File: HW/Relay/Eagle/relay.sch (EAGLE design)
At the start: 41 parts, among them IC2 DS18B20, K2 CQ1-12V, Q1A MMBT3904, Q1B MMBT3904, T1 BC847, U3 MCP16311

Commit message: Add files via upload
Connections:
- new net N$3: NC1.1, U3.VFB
- net N$28: no longer NC1.1, U3.VFB
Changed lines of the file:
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@@
 <wire x1="8.382" y1="264.16" x2="8.382" y2="267.716" width="0.1524" layer="91"/>
 <junction x="8.382" y="267.716"/>
-<pinref part="NC1" gate="G$1" pin="2"/>
-<wire x1="2.032" y1="263.906" x2="2.032" y2="267.716" width="0.1524" layer="91" style="shortdash"/>
-<junction x="2.032" y="267.716"/>
 <pinref part="SUPPLY11" gate="G$1" pin="VCC"/>
 <wire x1="-33.274" y1="281.432" x2="-33.274" y2="267.716" width="0.1524" layer="91"/>
 <junction x="-33.274" y="267.716"/>
 <pinref part="L1" gate="G$1" pin="1"/>
+<pinref part="NC1" gate="G$1" pin="2"/>
+<wire x1="2.032" y1="263.906" x2="2.032" y2="267.716" width="0.1524" layer="91"/>
+<junction x="2.032" y="267.716"/>
 </segment>
 <segment>
@@
 <net name="N$28" class="0">
 <segment>
-<pinref part="U3" gate="G$1" pin="VFB"/>
-<wire x1="75.184" y1="257.556" x2="75.184" y2="238.76" width="0.1524" layer="91"/>
-<wire x1="75.184" y1="238.76" x2="27.94" y2="238.76" width="0.1524" layer="91"/>
-<wire x1="27.94" y1="238.76" x2="27.94" y2="251.46" width="0.1524" layer="91"/>
 <pinref part="R15" gate="G$1" pin="1"/>
-<wire x1="27.94" y1="251.46" x2="8.382" y2="251.46" width="0.1524" layer="91"/>
-<wire x1="8.382" y1="251.46" x2="8.382" y2="254" width="0.1524" layer="91"/>
+<wire x1="8.382" y1="250.19" x2="8.382" y2="254" width="0.1524" layer="91"/>
 <pinref part="R16" gate="G$1" pin="2"/>
-<wire x1="8.382" y1="251.46" x2="8.382" y2="250.19" width="0.1524" layer="91"/>
-<pinref part="NC1" gate="G$1" pin="1"/>
-<wire x1="8.382" y1="251.46" x2="2.032" y2="251.46" width="0.1524" layer="91"/>
-<wire x1="2.032" y1="251.46" x2="2.032" y2="253.746" width="0.1524" layer="91"/>
 </segment>
 </net>
@@
 </segment>
 </net>
+<net name="N$3" class="0">
+<segment>
+<pinref part="NC1" gate="G$1" pin="1"/>
+<wire x1="2.032" y1="253.746" x2="2.032" y2="228.6" width="0.1524" layer="91"/>
+<wire x1="2.032" y1="228.6" x2="76.2" y2="228.6" width="0.1524" layer="91"/>
+<pinref part="U3" gate="G$1" pin="VFB"/>
+<wire x1="76.2" y1="228.6" x2="76.2" y2="257.556" width="0.1524" layer="91"/>
+<wire x1="76.2" y1="257.556" x2="75.184" y2="257.556" width="0.1524" layer="91"/>
+</segment>
+</net>

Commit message: Add files via upload
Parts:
- removed SV1: (no value), con-lsta:FE05-1
- added C6: 100nF, rcl:C-EUC0805
- added JP3: (no value), pinhead:PINHD-1X6
- added R1: 10k, antduino:SPARKFUN_RESISTOR0805-RES
- added R2: (no value), rcl:R-US_M2012
- added TP1, TP2, TP3, TP4, TP5, TP6: TPTP20SQ, testpad:TPTP20SQ
- R10: value (none) -> 10K
- R8: value (none) -> 1K
- R9: value (none) -> 4.7K
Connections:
- removed net N$17: SJR2.ADC
- net DTR: now also JP3.4; no longer SV1.5
- net GND: now also C6.1, JP3.6, TP6.TP; no longer SV1.1
- net PROG_IR_TR: now also R2.1, TP4.TP
- net RESET: now also C6.2, R1.2, TP5.TP
- net RTS: now also JP3.5; no longer SV1.2
- net RXD: now also JP3.2, TP2.TP; no longer SV1.4
- net TXD: now also JP3.3, TP3.TP; no longer SV1.3
- net VCC: now also R1.1, R2.2
- net VIN: now also JP3.1, TP1.TP

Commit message: Add files via upload
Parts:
- added R11, R12, R5: 10K, rcl:R-US_M2012
- added R14: 470, antduino:SPARKFUN_RESISTOR0805-RES
- added STATE_LED: (no value), led:LED3MM
- added U$2: DBCONN-1X2, Terminal Block Connector:DBCONN-1X2
- R2: value (none) -> 10K
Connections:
- new net ADC: R11.2, R12.2, SJR2.ADC
- new net N$11: R5.1, U$2.P1
- new net N$12: R11.1, U$2.P0
- new net N$4: R14.2, STATE_LED.A
- new net RXD1: SJR2.GPIO4, STATE_LED.C
- net GND: now also R12.1
- net VCC: now also R14.1, R5.2
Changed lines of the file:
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@@
 <part name="GND3" library="supply1" deviceset="GND" device=""/>
 <part name="SUPPLY13" library="SparkFun-Aesthetics" deviceset="VCC" device=""/>
-<part name="R2" library="rcl" library_urn="urn:adsk.eagle:library:334" deviceset="R-US_" device="M2012" package3d_urn="urn:adsk.eagle:package:23561/2"/>
+<part name="R2" library="rcl" library_urn="urn:adsk.eagle:library:334" deviceset="R-US_" device="M2012" package3d_urn="urn:adsk.eagle:package:23561/2" value="10K"/>
 <part name="P+2" library="supply1" library_urn="urn:adsk.eagle:library:371" deviceset="VCC" device=""/>
 <part name="JP3" library="pinhead" library_urn="urn:adsk.eagle:library:325" deviceset="PINHD-1X6" device="" package3d_urn="urn:adsk.eagle:package:22472/2"/>
+<part name="R14" library="antduino" deviceset="SPARKFUN_RESISTOR" device="0805-RES" value="470"/>
+<part name="SUPPLY9" library="SparkFun-Aesthetics" deviceset="VCC" device=""/>
+<part name="STATE_LED" library="led" library_urn="urn:adsk.eagle:library:259" deviceset="LED" device="3MM" package3d_urn="urn:adsk.eagle:package:15797/1"/>
+<part name="P+3" library="supply1" library_urn="urn:adsk.eagle:library:371" deviceset="VCC" device=""/>
+<part name="R5" library="rcl" library_urn="urn:adsk.eagle:library:334" deviceset="R-US_" device="M2012" package3d_urn="urn:adsk.eagle:package:23561/2" value="10K"/>
+<part name="R11" library="rcl" library_urn="urn:adsk.eagle:library:334" deviceset="R-US_" device="M2012" package3d_urn="urn:adsk.eagle:package:23561/2" value="10K"/>
+<part name="GND5" library="supply1" library_urn="urn:adsk.eagle:library:371" deviceset="GND" device=""/>
+<part name="U$2" library="Terminal Block Connector" deviceset="DBCONN-1X2" device=""/>
+<part name="R12" library="rcl" library_urn="urn:adsk.eagle:library:334" deviceset="R-US_" device="M2012" package3d_urn="urn:adsk.eagle:package:23561/2" value="10K"/>
 </parts>
 <sheets>
@@
 <attribute name="NAME" x="72.39" y="-177.165" size="1.778" layer="95"/>
 <attribute name="VALUE" x="72.39" y="-198.12" size="1.778" layer="96"/>
+</instance>
+<instance part="R14" gate="G$1" x="50.8" y="2.54" smashed="yes" rot="R270">
+<attribute name="NAME" x="52.2986" y="6.35" size="1.778" layer="95" rot="R270"/>
+<attribute name="VALUE" x="47.498" y="6.35" size="1.778" layer="96" rot="R270"/>
+</instance>
+<instance part="SUPPLY9" gate="G$1" x="50.8" y="10.16" smashed="yes">
+<attribute name="VALUE" x="49.784" y="13.716" size="1.778" layer="96"/>
+</instance>
+<instance part="STATE_LED" gate="G$1" x="50.8" y="-7.62" smashed="yes">
+<attribute name="NAME" x="54.356" y="-14.732" size="1.778" layer="95" rot="R90"/>
+<attribute name="VALUE" x="56.515" y="-12.192" size="1.778" layer="96" rot="R90"/>
+</instance>
+<instance part="P+3" gate="VCC" x="109.22" y="-55.88" smashed="yes" rot="R270">
+<attribute name="VALUE" x="106.68" y="-53.34" size="1.778" layer="96"/>
+</instance>
+<instance part="R5" gate="G$1" x="81.28" y="-55.88" smashed="yes">
+<attribute name="NAME" x="77.47" y="-54.3814" size="1.778" layer="95"/>
+<attribute name="VALUE" x="77.47" y="-59.182" size="1.778" layer="96"/>
+</instance>
+<instance part="R11" gate="G$1" x="73.66" y="-66.04" smashed="yes">
+<attribute name="NAME" x="69.85" y="-64.5414" size="1.778" layer="95"/>
+<attribute name="VALUE" x="69.85" y="-69.342" size="1.778" layer="96"/>
+</instance>
+<instance part="GND5" gate="1" x="83.82" y="-93.98" smashed="yes">
+<attribute name="VALUE" x="81.28" y="-96.52" size="1.778" layer="96"/>
+</instance>
+<instance part="U$2" gate="G$1" x="50.8" y="-60.96" smashed="yes" rot="R180"/>
+<instance part="R12" gate="G$1" x="83.82" y="-78.74" smashed="yes" rot="R90">
+<attribute name="NAME" x="82.3214" y="-82.55" size="1.778" layer="95" rot="R90"/>
+<attribute name="VALUE" x="87.122" y="-82.55" size="1.778" layer="96" rot="R90"/>
 </instance>
 </instances>
@@
 <wire x1="76.2" y1="-193.04" x2="53.34" y2="-193.04" width="0.1524" layer="91"/>
 <label x="53.34" y="-193.04" size="1.016" layer="95" rot="R180" xref="yes"/>
+</segment>
+<segment>
+<pinref part="R12" gate="G$1" pin="1"/>
+<pinref part="GND5" gate="1" pin="GND"/>
+<wire x1="83.82" y1="-83.82" x2="83.82" y2="-91.44" width="0.1524" layer="91"/>
 </segment>
 </net>
@@
 <wire x1="25.4" y1="12.7" x2="25.4" y2="7.62" width="0.1524" layer="91"/>
 </segment>
+<segment>
+<pinref part="R14" gate="G$1" pin="1"/>
+<pinref part="SUPPLY9" gate="G$1" pin="VCC"/>
+<wire x1="50.8" y1="10.16" x2="50.8" y2="7.62" width="0.1524" layer="91"/>
+</segment>
+<segment>
+<pinref part="R5" gate="G$1" pin="2"/>
+<pinref part="P+3" gate="VCC" pin="VCC"/>
+<wire x1="86.36" y1="-55.88" x2="106.68" y2="-55.88" width="0.1524" layer="91"/>
+</segment>
 </net>
 <net name="VIN" class="0">
@@
 <wire x1="40.64" y1="106.68" x2="40.64" y2="96.52" width="0.1524" layer="91"/>
 <pinref part="SG4" gate="G$1" pin="+"/>
+<label x="25.4" y="129.54" size="1.27" layer="95" rot="R90" xref="yes"/>
+<label x="25.4" y="129.54" size="1.27" layer="95" rot="R90" xref="yes"/>
 </segment>
 </net>
@@
 </segment>
 </net>
+<net name="RXD1" class="0">
+<segment>
+<pinref part="STATE_LED" gate="G$1" pin="C"/>
+<wire x1="50.8" y1="-12.7" x2="50.8" y2="-27.94" width="0.1524" layer="91"/>
+<pinref part="SJR2" gate="G$1" pin="GPIO4"/>
+<wire x1="22.86" y1="-27.94" x2="50.8" y2="-27.94" width="0.1524" layer="91"/>
+</segment>
+</net>
+<net name="N$4" class="0">
+<segment>
+<pinref part="R14" gate="G$1" pin="2"/>
+<pinref part="STATE_LED" gate="G$1" pin="A"/>
+<wire x1="50.8" y1="-5.08" x2="50.8" y2="-2.54" width="0.1524" layer="91"/>
+</segment>
+</net>
+<net name="ADC" class="0">
+<segment>
+<pinref part="SJR2" gate="G$1" pin="ADC"/>
+<wire x1="-10.16" y1="-22.86" x2="-15.24" y2="-22.86" width="0.1524" layer="91"/>
+<label x="-15.24" y="-22.86" size="1.778" layer="95" rot="R180" xref="yes"/>
+</segment>
+<segment>
+<pinref part="R12" gate="G$1" pin="2"/>
+<pinref part="R11" gate="G$1" pin="2"/>
+<wire x1="83.82" y1="-73.66" x2="83.82" y2="-66.04" width="0.1524" layer="91"/>
+<wire x1="83.82" y1="-66.04" x2="78.74" y2="-66.04" width="0.1524" layer="91"/>
+<wire x1="83.82" y1="-66.04" x2="91.44" y2="-66.04" width="0.1524" layer="91"/>
+<junction x="83.82" y="-66.04"/>
+<label x="91.44" y="-66.04" size="1.778" layer="95" xref="yes"/>
+</segment>
+</net>
+<net name="N$12" class="0">
+<segment>
+<pinref part="R11" gate="G$1" pin="1"/>
+<wire x1="68.58" y1="-66.04" x2="63.5" y2="-66.04" width="0.1524" layer="91"/>
+<pinref part="U$2" gate="G$1" pin="P0"/>
+<wire x1="63.5" y1="-66.04" x2="63.5" y2="-63.5" width="0.1524" layer="91"/>
+<wire x1="63.5" y1="-63.5" x2="55.88" y2="-63.5" width="0.1524" layer="91"/>
+</segment>
+</net>
+<net name="N$11" class="0">
+<segment>
+<pinref part="R5" gate="G$1" pin="1"/>
+<wire x1="76.2" y1="-55.88" x2="63.5" y2="-55.88" width="0.1524" layer="91"/>
+<wire x1="63.5" y1="-55.88" x2="63.5" y2="-58.42" width="0.1524" layer="91"/>
+<pinref part="U$2" gate="G$1" pin="P1"/>
+<wire x1="63.5" y1="-58.42" x2="55.88" y2="-58.42" width="0.1524" layer="91"/>
+</segment>
+</net>

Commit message: relay_sch updated.
Relay sch, Programming sch, sch. image are updated.
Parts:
- removed C11, C14: 100nF, rcl:C-EUC0805
- removed C13: 10uF, rcl:C-EUC0805
- removed JP3: (no value), pinhead:PINHD-1X6
- removed NC1: (no value), antduino:SPARKFUN_RESISTOR0805-RES
- removed Q1A, Q1B: MMBT3904, MMBT3904:MMBT3904
- removed R3, R4, R6, R7: 10k, antduino:SPARKFUN_RESISTOR0805-RES
- added NC: (no value), antduino:SPARKFUN_RESISTOR0805-RES
- D3: value 1A/40V/500mV -> S514
- R9: value 4.7K -> 4k7
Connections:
- net DS18B20 renamed HEAT_S
- removed net DTR: JP3.4, Q1A.E, R6.2
- removed net N$2: Q1A.B, R4.1
- removed net N$28: R15.1, R16.2
- removed net N$6: Q1B.B, R6.1
- removed net PROG_IR_TR: Q1A.C, R2.1, R3.1, SJR2.GPIO0, TP4.TP
- removed net RTS: JP3.5, Q1B.E, R4.2
- new net IR_TX: R2.1, SJR2.GPIO0, TP4.TP
- net GND: no longer C11.1, C13.1, C14.1, JP3.6
- net N$3: now also NC.1, R15.1, R16.2; no longer NC1.1
- net RESET: no longer C11.2, Q1B.C, R7.1
- net RXD: no longer JP3.2
- net TXD: no longer JP3.3
- net VCC: now also NC.2; no longer C13.2, C14.2, NC1.2, R3.2, R7.2
- net VIN: no longer JP3.1
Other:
- note added: "03.04.2020"
- note added: "BUTTON_CONN"
- note added: "CHECK !"
- note added: "ESP-12 based Relay"
- note added: "ESP12E Module"
- note added: "Heat Sensor"
- note added: "POWER"
- note added: "Programming Socket"
- note added: "RELAY"
- note added: "RF MODULE"
- note added: "Relay Inside"
- note added: "Wifi_DoorLock_Project"
- moved on the sheet: C1, C15, C16, C17, C18, C19, C2, C21, C22, C23, C3, C4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

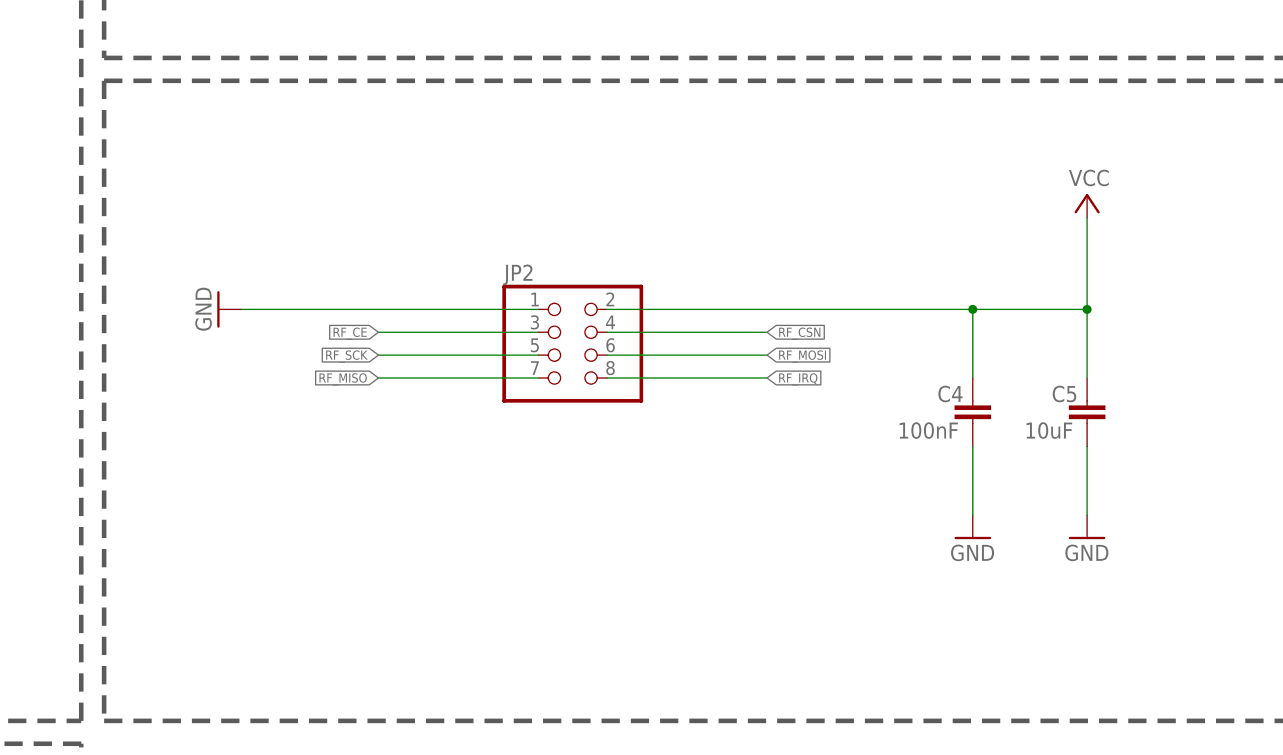
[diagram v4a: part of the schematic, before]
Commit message: Update relay.sch
NRF24L01 module has changed.
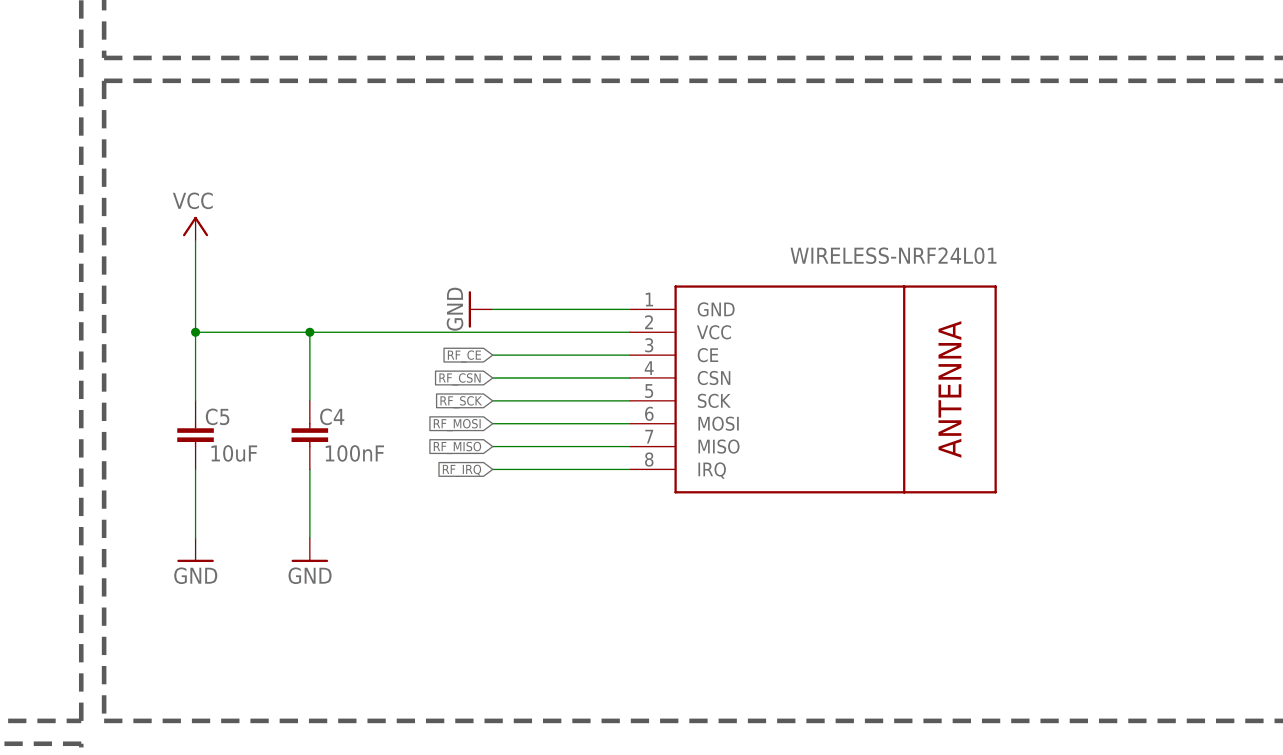
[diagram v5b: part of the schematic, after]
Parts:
- removed JP2: (no value), adafruit:PINHD-2X4
- added M1: WIRELESS-NRF24L01, diy-modules:WIRELESS-NRF24L01
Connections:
- net GND: now also M1.GND; no longer JP2.1
- net RF_CE: now also M1.CE; no longer JP2.3
- net RF_CSN: now also M1.CSN; no longer JP2.4
- net RF_IRQ: now also M1.IRQ; no longer JP2.8
- net RF_MISO: now also M1.MISO; no longer JP2.7
- net RF_MOSI: now also M1.MOSI; no longer JP2.6
- net RF_SCK: now also M1.SCK; no longer JP2.5
- net VCC: now also M1.VCC; no longer JP2.2
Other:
- moved on the sheet: C4, C5

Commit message: Add files via upload
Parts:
- removed JP1: (no value), pinhead:PINHD-1X3
- removed R2: 10K, rcl:R-US_M2012
- removed U$1, U$2: DBCONN-1X2, Terminal Block Connector:DBCONN-1X2
- added J1, J2: 284513-2, 284513-2:284513-2
- added J3: 284513-3, 284513-3:284513-3
- R11, R5: value 10K -> 4.7K
- R12: value 10K -> 3.3K
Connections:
- removed net ADC: R11.2, R12.2, SJR2.ADC
- removed net RXD1: SJR2.GPIO4, STATE_LED.C
- new net BUTTON_CONTROL: R11.2, R12.2, SJR2.GPIO4
- net C: now also J3.2; no longer JP1.2
- net GND: now also J1.2; no longer U$1.P1
- net IR_TX: no longer R2.1, SJR2.GPIO0
- net N$11: now also J2.2; no longer U$2.P1
- net N$12: now also J2.1; no longer U$2.P0
- net NC: now also J3.3; no longer JP1.1
- net NO: now also J3.1; no longer JP1.3
- net RF_CE: now also SJR2.GPIO2; no longer SJR2.GPIO15
- net RF_CSN: now also SJR2.GPIO15; no longer SJR2.GPIO2
- net RF_IRQ: now also SJR2.GPIO0
- net TXD: now also STATE_LED.C
- net VCC: no longer R2.2
- net VIN: now also J1.1; no longer U$1.P0
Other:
- note added: "12 V Buzzer !"
- moved on the sheet: R14, STATE_LED
